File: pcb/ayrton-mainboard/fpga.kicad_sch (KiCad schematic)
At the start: 1 part, among them U2 XC7K160T-2FFG676C

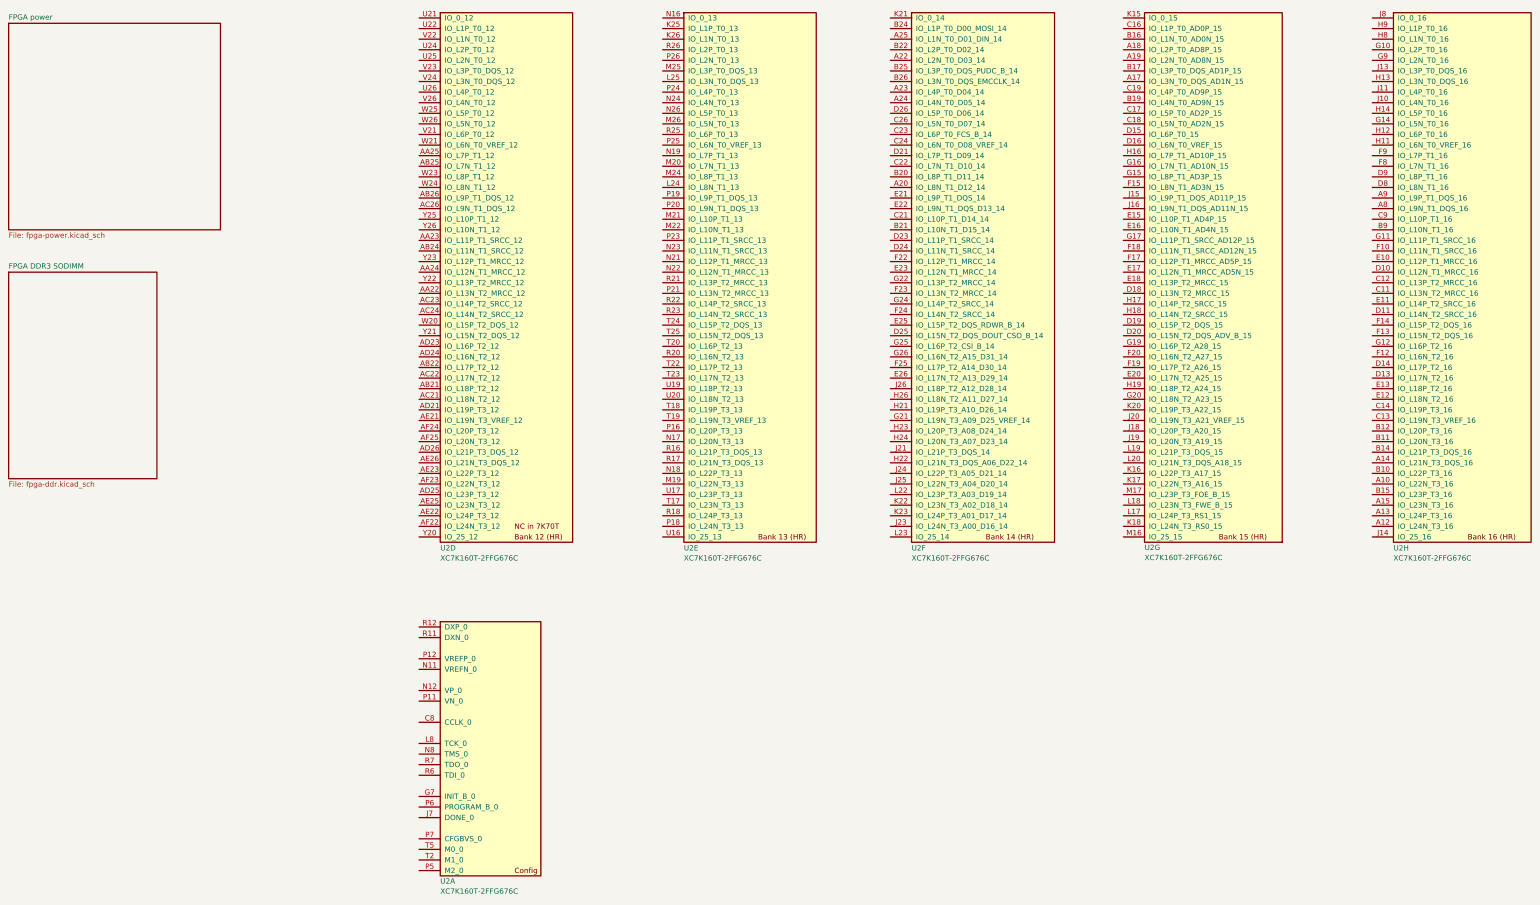
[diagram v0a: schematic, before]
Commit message: Continued initial schematic, working on LPDDR4
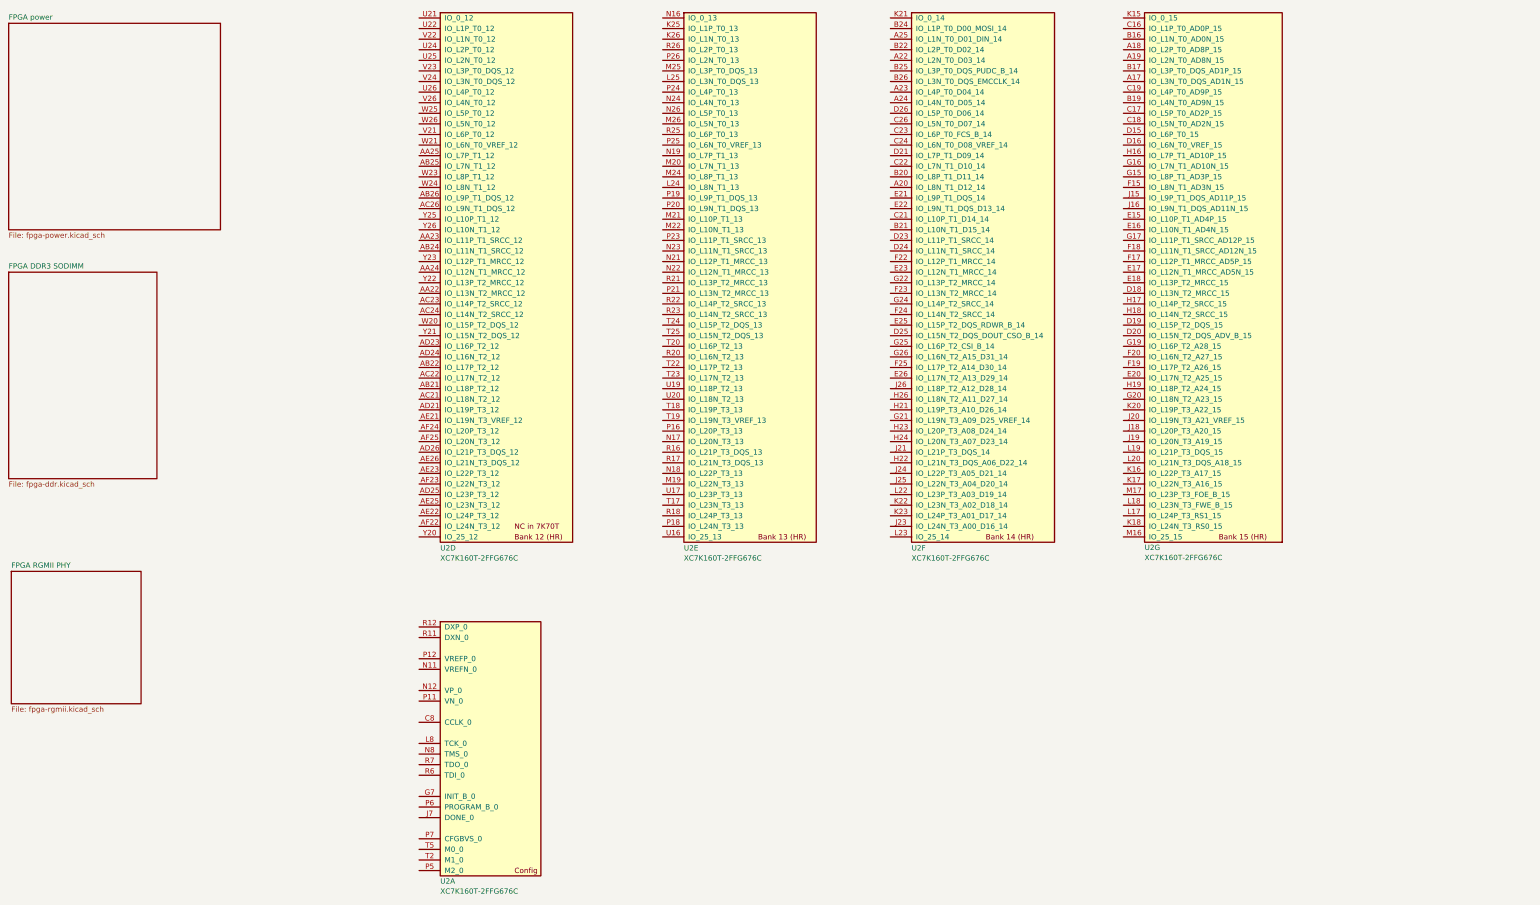
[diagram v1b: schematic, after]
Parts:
- removed unit 8 of U2
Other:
- added sheet FPGA RGMII PHY (fpga-rgmii.kicad_sch)
